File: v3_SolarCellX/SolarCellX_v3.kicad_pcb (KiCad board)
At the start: 6 copper layers, 48.4 x 48.4 mm, 47 parts, among them J1 XF2M-1015-1A, U1 Value, U2 TSL2561

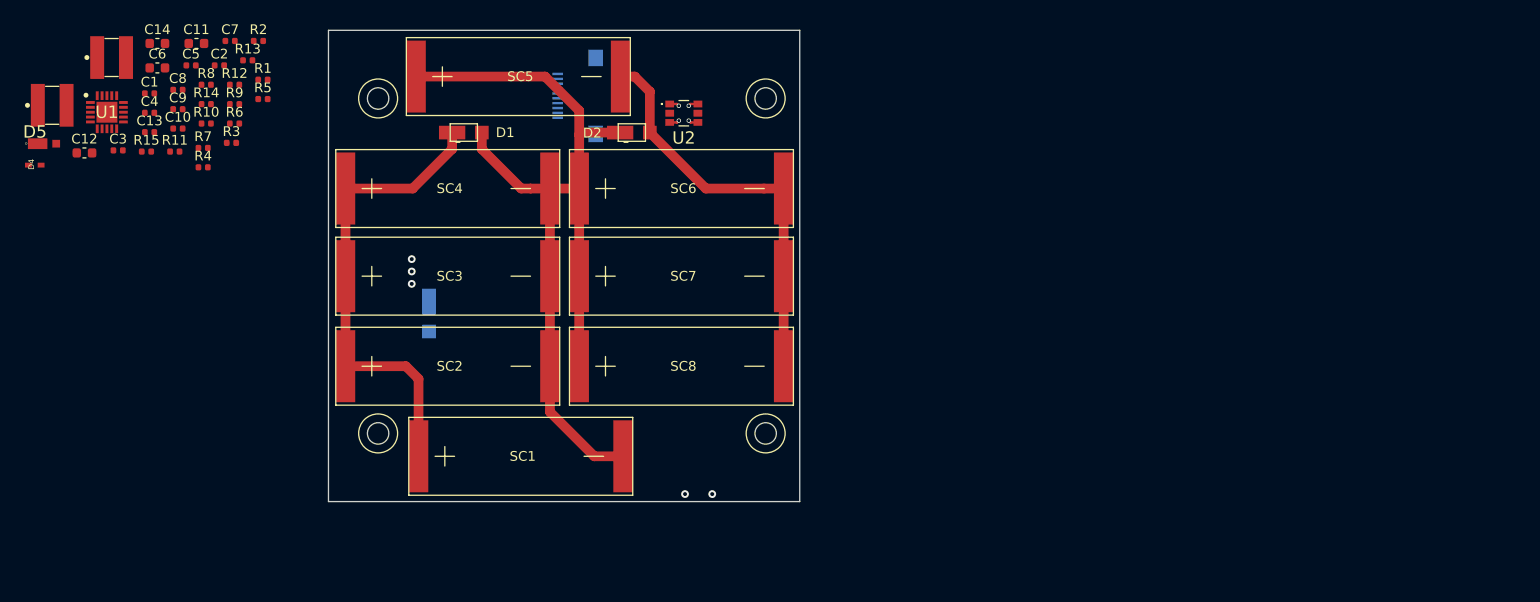
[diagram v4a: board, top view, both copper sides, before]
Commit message: circuits added and coil connection made
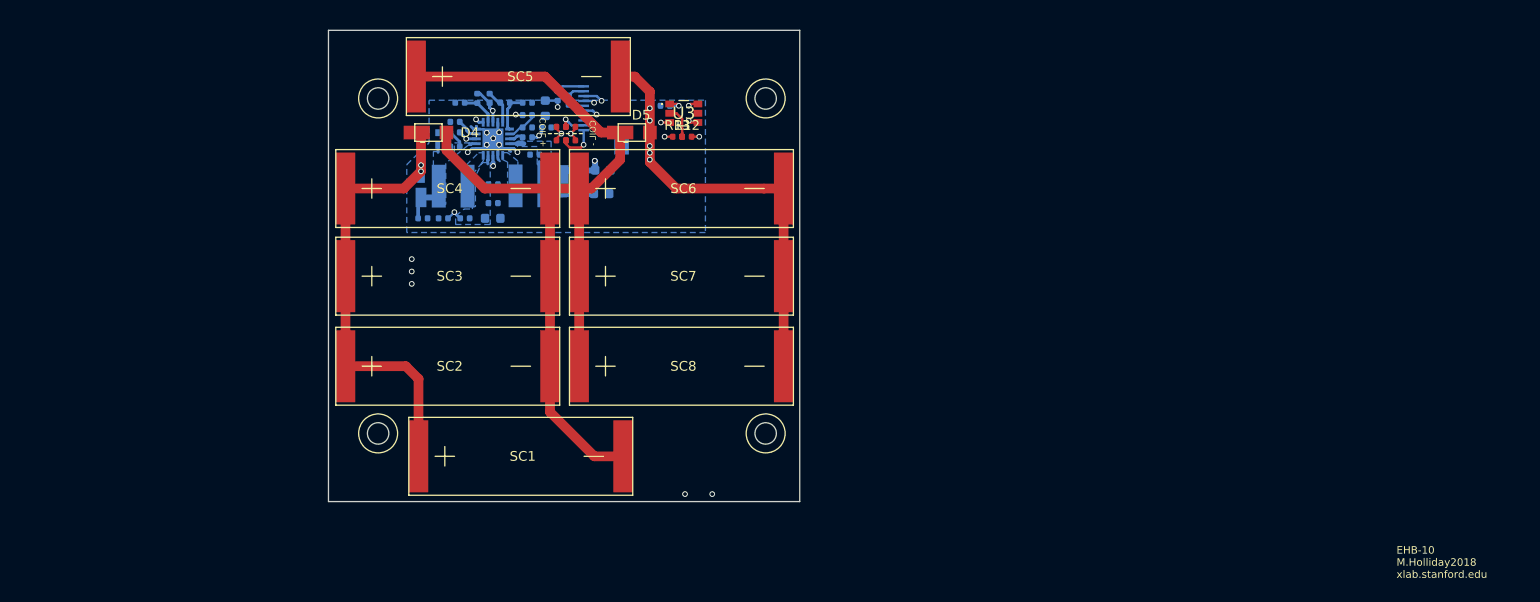
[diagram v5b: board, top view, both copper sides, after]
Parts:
- removed the D4 at (59.8, 53.8)
- removed the D5 at (60.8, 51.6)
- removed U1: Value, misc-circuits:QFN50P350X350X100-21N-D
- added D1: SDM20U40-7, misc-circuits:SOD523, B.Cu at (101.2, 51.2)
- added D2: MSS1P4-M3_89A, custom-footprints:MICROSMP, B.Cu at (114.1, 55.5)
- added R16: 0, Resistor_SMD:R_0402_1005Metric, B.Cu at (104.0, 59.3)
- added R17: 0, Resistor_SMD:R_0402_1005Metric, B.Cu at (113.5, 46.7)
- added R18: 0, Resistor_SMD:R_0402_1005Metric, B.Cu at (114.7, 47.2)
- added R19: 0, Resistor_SMD:R_0402_1005Metric, F.Cu at (114.9, 49.9)
- added U3: TSL2561, misc-circuits:TSL2561, F.Cu at (126.5, 48.5)
- C1: value 0.1uF -> 1.0uF; moved to B.Cu
- C10, C11, C12, C13, C14, C6, C7, C8, C9, L1, L2, R1, R14, R15: moved to B.Cu
- C2: value 1.0uF -> 0.1uF; moved to B.Cu
- C3: value 0.1uF -> 4.7uF; moved to B.Cu
- C4: value 4.7uF -> 10nF; moved to B.Cu
- C5: value 10nF -> 0.1uF; moved to B.Cu
- D3: value SBDiode -> MSS1P4-M3_89A; footprint SolarCellParts:SB Diode -> custom-footprints:MICROSMP
- J1: footprint misc-circuits:XF2M-1015-1A -> custom-footprints:XF2M-1015-1A
- R10: value 4.75M -> 8.25M; moved to B.Cu
- R11: value 0 -> 4.75M; moved to B.Cu
- R4: value 7.32M -> 0
- R5: value 5.62M -> 7.32M; moved to B.Cu
- R6: value 374K -> 5.62M; moved to B.Cu
- R7: value 8.25M -> 374K; moved to B.Cu
- R8: value 4.53M -> 8.25M; moved to B.Cu
- R9: value 8.25M -> 4.53M; moved to B.Cu
- U2: value TSL2561 -> Value; footprint misc-circuits:TSL2561 -> misc-circuits:QFN50P350X350X100-21N-D; moved to B.Cu
- moved C12 53.3 mm to (118.0, 56.8)
- moved L2 49.8 mm to (110.7, 56.0)
- moved C5 48.9 mm to (124.6, 47.8)
- moved C14 47.6 mm to (118.2, 54.4)
- moved R12 46.8 mm to (126.8, 50.9)
- moved R13 44.8 mm to (125.8, 50.9)
- moved C13 44.3 mm to (115.8, 53.9), turned to 90 degrees
- moved C10 41.7 mm to (115.8, 56.3), turned to 90 degrees
- moved C1 40.9 mm to (112.4, 50.0)
- moved C6 40.1 mm to (112.3, 48.0), turned to 270 degrees
- moved L1 37.5 mm to (102.8, 56.0)
- moved R4 37.0 mm to (113.9, 49.9), turned to 180 degrees
- moved R11 36.3 mm to (110.4, 50.0), turned to 180 degrees
- moved C11 35.3 mm to (106.9, 59.3)
- moved R3 34.8 mm to (114.9, 51.3), turned to 180 degrees
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- renumbered D1 to D4, D2 to D5
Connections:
- C1 pad 1: GND -> VOUT_EN
- C1 pad 2: +3V3 -> GND
- C2 pad 1: VOUT_EN -> VSOLAR
- C4 pad 1: VSOLAR -> Net-(C4-Pad1)
- C5 pad 1: Net-(C5-Pad1) -> GND
- C5 pad 2: GND -> +3V3
- D3 pad 1: VSolar -> VSOLAR
- J1 pad 1: SDA1 -> BATT_P
- J1 pad 10: GND -> COIL_P
- J1 pad 2: BATT_P -> BATT_N
- J1 pad 3: SCL1 -> SDA1
- J1 pad 4: BATT_N -> SCL1
- J1 pad 6: COIL_P -> +3V3
- J1 pad 7: +3V3 -> GND
- J1 pad 8: COIL_N -> GND
- J1 pad 9: GND -> COIL_N
- R1 pad 1: Net-(R1-Pad1) -> VBAT_OK
- R1 pad 2: +3V3 -> VOUT_EN
- R10 pad 1: GND -> Net-(R10-Pad1)
- R11 pad 1: Net-(R11-Pad1) -> GND
- R11 pad 2: VSOLAR -> Net-(R10-Pad1)
- R12 pad 1: GND -> Net-(R12-Pad1)
- R12 pad 2: Net-(R11-Pad1) -> +3V3
- R13 pad 1: Net-(C11-Pad1) -> GND
- R13 pad 2: Net-(R11-Pad1) -> Net-(R12-Pad1)
- R14 pad 1: BATT_P -> Net-(R14-Pad1)
- R14 pad 2: /VBAT -> VSOLAR
- R15 pad 1: BATT_N -> GND
- R15 pad 2: GND -> Net-(R14-Pad1)
- R2 pad 1: GND -> COIL_P
- R2 pad 2: Net-(R1-Pad1) -> /coil
- R3 pad 1: VBAT_OK -> /coil
- R3 pad 2: VOUT_EN -> COIL_P
- R4 pad 1: Net-(R4-Pad1) -> COIL_N
- R4 pad 2: Net-(R4-Pad2) -> /coil
- R5 pad 1: GND -> Net-(R5-Pad1)
- R5 pad 2: Net-(R4-Pad1) -> Net-(R10-Pad2)
- R6 pad 1: Net-(R6-Pad1) -> GND
- R6 pad 2: Net-(R4-Pad2) -> Net-(R5-Pad1)
- R7 pad 2: Net-(R6-Pad1) -> Net-(R10-Pad2)
- R8 pad 1: GND -> Net-(R8-Pad1)
- R9 pad 1: Net-(R10-Pad2) -> GND
- R9 pad 2: Net-(R4-Pad2) -> Net-(R8-Pad1)
- U2 pad 1: +3V3 -> GND
- U2 pad 2: Net-(R1-Pad1) -> VSOLAR
- U2 pad 3: GND -> Net-(R14-Pad1)
- U2 pad 4: SCL1 -> Net-(C4-Pad1)
- U2 pad 5: Net-(U2-Pad5) -> GND
- U2 pad 6: SDA1 -> VOUT_EN
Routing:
- net /coil: track 0.00 -> 16389.4 mm, vias 0 -> 7
- net (no net): track 16333.0 -> 0.00 mm, vias 5 -> 0
- net +3V3: track 1.02 -> 26.8 mm, vias 1 -> 4
- net GND: track 43.2 -> 58.1 mm, vias 1 -> 14
- net /VBAT: track 0.00 -> 13.9 mm, vias 0 -> 2
- net SCL1: track 1.02 -> 13.9 mm, vias 1 -> 2
- net Net-(R14-Pad1): track 0.00 -> 11.8 mm, vias 0 -> 2
- net SDA1: track 1.02 -> 12.7 mm, vias 1 -> 2
- net VOUT_EN: track 0.00 -> 9.76 mm, vias 0 -> 2
- net Net-(C10-Pad1): track 0.00 -> 9.20 mm
- net Net-(R10-Pad2): track 0.00 -> 7.04 mm, vias 0 -> 2
- net VSOLAR: track 0.00 -> 6.82 mm
- net Net-(D4-Pad2): track 94.7 -> 99.2 mm
- net Net-(R8-Pad1): track 0.00 -> 4.22 mm
- net COIL_P: track 0.00 -> 4.01 mm, vias 0 -> 1
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- added copper zone on B.Cu, net GND
- added copper zone on In3.Cu, net GND
- added copper zone on B.Cu, net Net-(C10-Pad1)
- added copper zone on B.Cu, net Net-(C11-Pad1)
- added copper zone on B.Cu, net Net-(L1-Pad2)
- added copper zone on B.Cu, net Net-(L2-Pad1)
- added copper zone on B.Cu, net VSOLAR
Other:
- net class Default: trace_width 0.249936 -> 0.2286; via_dia 0.45 -> 0.5842; via_drill 0.3 -> 0.381
- rule trace_min: 0.127 -> 0.1524
- board text added: "1"
- board text added: "20"
- board text added: "3.3V OUT"
- board text added: "5V EN"
- board text added: "5V OUT"
- board text added: "COIL +"
- board text added: "COIL -"
- board text added: "DNI"
- board text added: "EHB-10 M.Holliday2018 xlab.stanford.edu"
- board text added: "EXT BAT"
- board text added: "SOLAR IN"
- board text added: "VBAT OK"
- board text added: "VBAT_0V"
- board text added: "VBAT_OK"
- board text added: "VOUT"
- board text added: "VOUT EN"

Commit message: cleanup- still need to add logo
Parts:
- C5: moved to F.Cu
- moved C5 0.77 mm to (123.9, 48.1), turned to 90 degrees
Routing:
- net COIL_N: track 2.80 -> 3.97 mm
- net GND: track 58.1 -> 59.1 mm
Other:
- board text added: "+"
- board text added: "-"
- board text added: "3V3"
- board text added: "GND"
- board text added: "N"
- board text added: "P"
- board text removed: "1"
- board text removed: "20"
- board text removed: "3.3V OUT"
- board text removed: "5V EN"
- board text removed: "5V OUT"
- board text removed: "COIL +"
- board text removed: "COIL -"
- board text removed: "DNI"
- board text removed: "EHB-10 M.Holliday2018 xlab.stanford.edu"
- board text removed: "EXT BAT"
- board text removed: "SOLAR IN"
- board text removed: "VBAT OK"
- board text removed: "VBAT_0V"
- board text removed: "VBAT_OK"
- board text removed: "VOUT"
- board text removed: "VOUT EN"

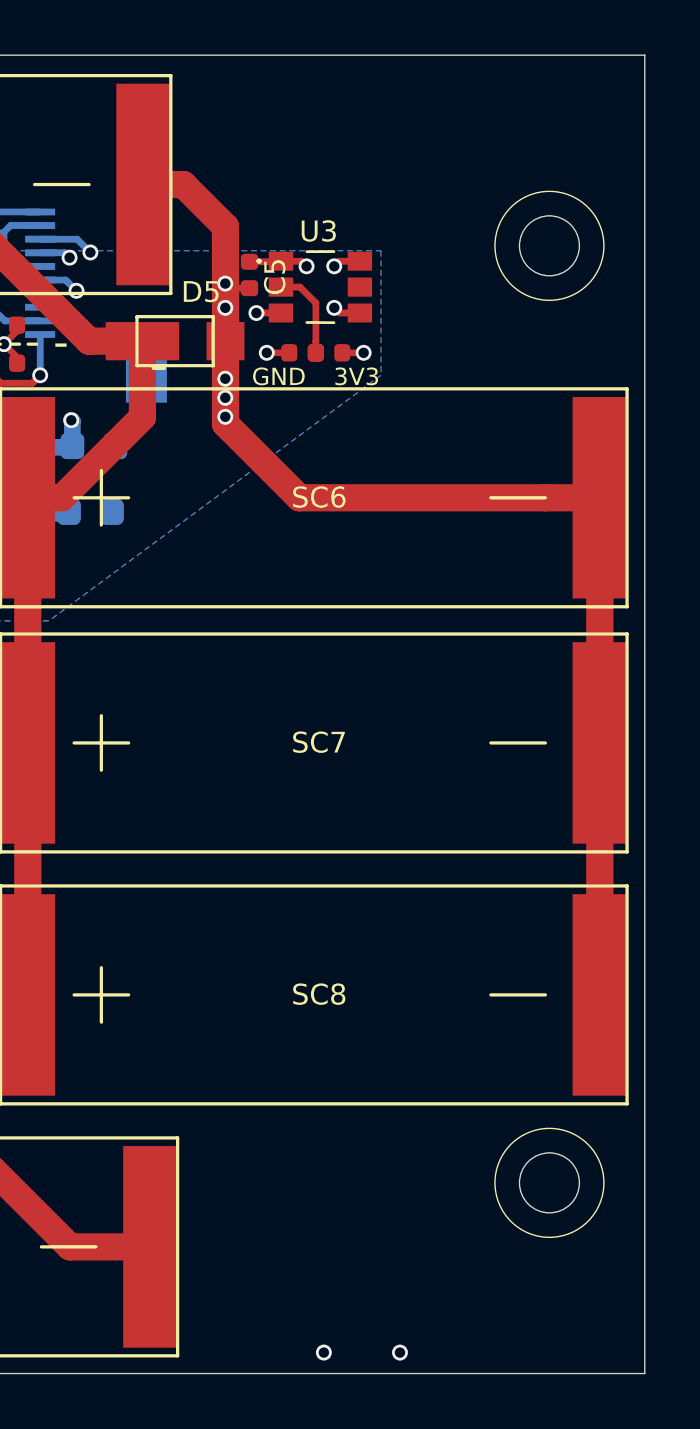
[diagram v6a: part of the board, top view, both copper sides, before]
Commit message: X and Z panels are ready
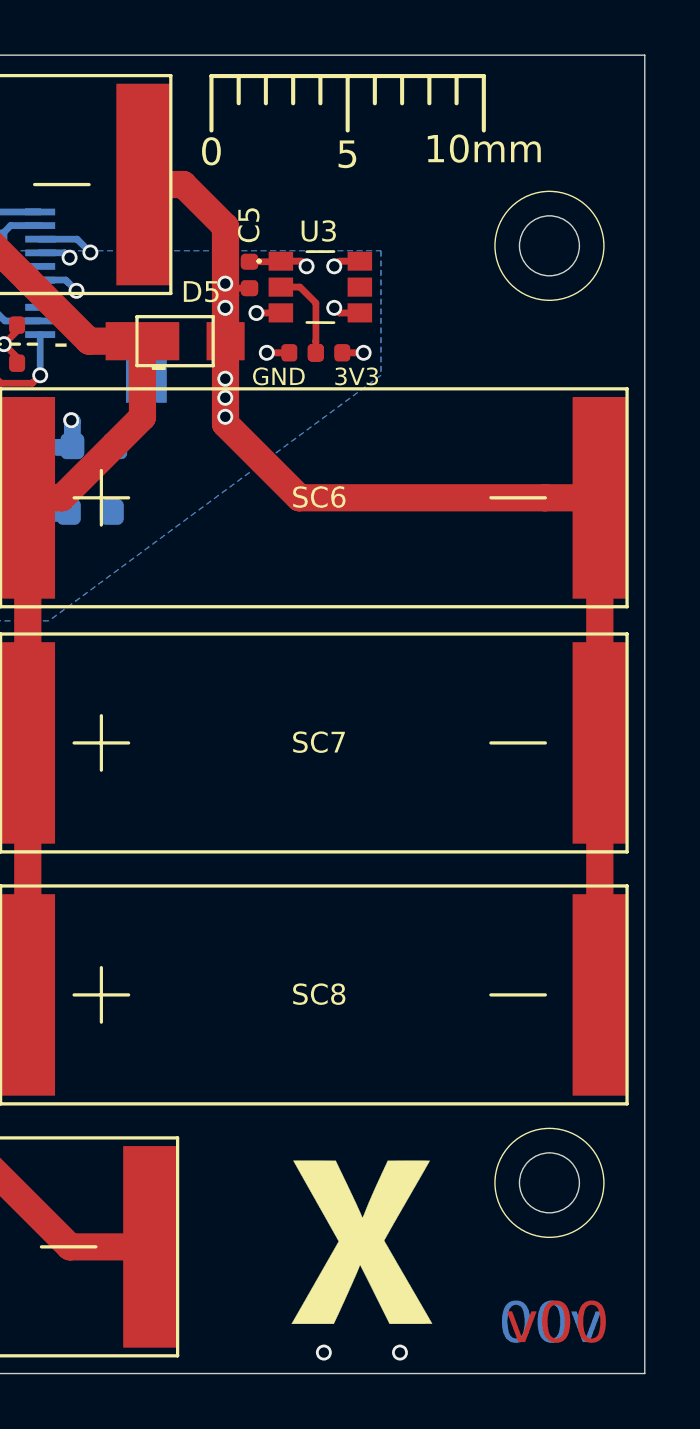
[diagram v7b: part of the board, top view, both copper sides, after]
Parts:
- added REF**: Gauge_10mm_Type1_SilkScreenTop, Calibration_Scale:Gauge_10mm_Type1_SilkScreenTop, F.Cu at (122.5, 40.8)
- added Ref**: Val**, custom-footprints:xpanel, F.Cu at (144.8, 82.6)
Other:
- board text added: "v00"

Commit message: zipped fabrication files for all but +Y
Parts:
- removed REF**: Gauge_10mm_Type1_SilkScreenTop, Calibration_Scale:Gauge_10mm_Type1_SilkScreenTop
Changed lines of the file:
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@@
     (tracks 1306)
     (zones 0)
-    (modules 53)
+    (modules 52)
     (nets 30)
   )
   (page A4)
   (layers
-    (0 Top signal hide)
-    (1 In1.Cu signal hide)
-    (2 In2.Cu signal hide)
+    (0 Top signal)
+    (1 In1.Cu signal)
+    (2 In2.Cu signal)
     (3 In3.Cu signal)
-    (4 In4.Cu signal hide)
+    (4 In4.Cu signal)
     (31 Bottom signal)
     (32 B.Adhes user hide)
@@
     (34 B.Paste user hide)
     (35 F.Paste user hide)
-    (36 B.SilkS user hide)
-    (37 F.SilkS user hide)
+    (36 B.SilkS user)
+    (37 F.SilkS user)
     (38 B.Mask user)
     (39 F.Mask user)
@@
     (pcbplotparams
       (layerselection 0x010fc_ffffffff)
-      (usegerberextensions false)
+      (usegerberextensions true)
       (usegerberattributes false)
       (usegerberadvancedattributes false)
       (creategerberjobfile false)
-      (excludeedgelayer true)
+      (excludeedgelayer false)
       (linewidth 0.100000)
       (plotframeref false)
@@
       (outputformat 1)
       (mirror false)
-      (drillshape 1)
+      (drillshape 0)
       (scaleselection 1)
       (outputdirectory ""))
@@
     (add_net VSOLAR)
   )
-  (module Calibration_Scale:Gauge_10mm_Type1_SilkScreenTop (layer Top)
-    (at 122.4915 40.767)
-    (descr "Gauge, Massstab, 10mm, SilkScreenTop, Type 1,")
-    (tags "Gauge Massstab 10mm SilkScreenTop Type 1")
-    (attr virtual)
-    (fp_text reference REF** (at 0 -2.99974) (layer F.SilkS) hide
-      (effects (font (size 1 1) (thickness 0.15)))
-    )
-    (fp_text value Gauge_10mm_Type1_SilkScreenTop (at 10.20064 4.8006) (layer F.Fab)
-      (effects (font (size 1 1) (thickness 0.15)))
-    )
-    (fp_line (start 9.99998 0) (end 9.99998 1.99898) (layer F.SilkS) (width 0.15))
-    (fp_line (start 0 0) (end 9.99998 0) (layer F.SilkS) (width 0.15))
-    (fp_line (start 0 0) (end 0 1.99898) (layer F.SilkS) (width 0.15))
-    (fp_line (start 5.00126 0) (end 5.00126 1.99898) (layer F.SilkS) (width 0.15))
-    (fp_line (start 1.00076 0) (end 1.00076 1.00076) (layer F.SilkS) (width 0.15))
-    (fp_line (start 1.99898 0) (end 1.99898 1.00076) (layer F.SilkS) (width 0.15))
-    (fp_line (start 2.99974 0) (end 2.99974 1.00076) (layer F.SilkS) (width 0.15))
-    (fp_line (start 4.0005 0) (end 4.0005 1.00076) (layer F.SilkS) (width 0.15))
-    (fp_line (start 5.99948 0) (end 5.99948 1.00076) (layer F.SilkS) (width 0.15))
-    (fp_line (start 7.00024 0) (end 7.00024 1.00076) (layer F.SilkS) (width 0.15))
-    (fp_line (start 8.001 0) (end 8.001 1.00076) (layer F.SilkS) (width 0.15))
-    (fp_line (start 8.99922 0) (end 8.99922 1.00076) (layer F.SilkS) (width 0.15))
-    (fp_text user 10mm (at 9.99998 2.70002) (layer F.SilkS)
-      (effects (font (size 1 1) (thickness 0.15)))
-    )
-    (fp_text user 0 (at 0 2.79908) (layer F.SilkS)
-      (effects (font (size 1 1) (thickness 0.15)))
-    )
-    (fp_text user 5 (at 4.99872 2.90068) (layer F.SilkS)
-      (effects (font (size 1 1) (thickness 0.15)))
-    )
-    (fp_text user %R (at 0 -2.99974) (layer F.Fab)
-      (effects (font (size 1 1) (thickness 0.15)))
-    )
-  )
   (module custom-footprints:xpanel (layer Top)
